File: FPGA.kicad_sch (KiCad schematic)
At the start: 14 parts, among them U3 XC7A100T-FTG256, U5 S25FL127S

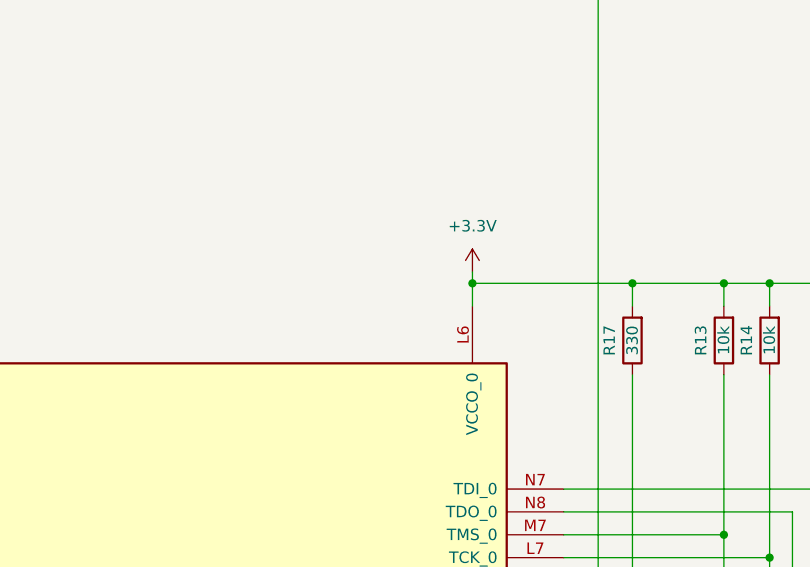
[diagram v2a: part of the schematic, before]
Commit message: Wired FPGA program to MCU
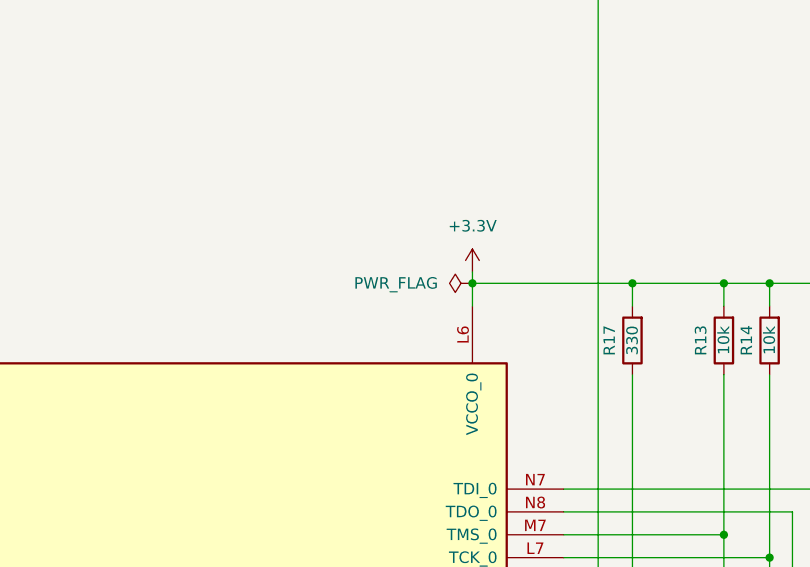
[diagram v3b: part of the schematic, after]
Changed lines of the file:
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@@
+    )
+  )
+  (symbol (lib_id "power:PWR_FLAG") (at 91.44 182.88 90) (unit 1)
+    (in_bom yes) (on_board yes) (dnp no) (fields_autoplaced)
+    (property "Reference" "#FLG04" (at 89.535 182.88 0)
+      (effects (font (size 1.27 1.27)) hide)
+    )
+    (property "Value" "PWR_FLAG" (at 87.63 182.88 90)
+      (effects (font (size 1.27 1.27)) (justify left))
+    )
+    (property "Footprint" "" (at 91.44 182.88 0)
+      (effects (font (size 1.27 1.27)) hide)
+    )
+    (property "Datasheet" "~" (at 91.44 182.88 0)
+      (effects (font (size 1.27 1.27)) hide)
+    )
+    (pin "1")
+    (instances
+      (project "GuitarZero"
+        (path "/fba50eda-8593-4456-af98-ff56fd418a76/7788bc9b-1e55-4835-b7d3-ea790efb8c61"
+          (reference "#FLG04") (unit 1)
+        )
+      )
     )
   )

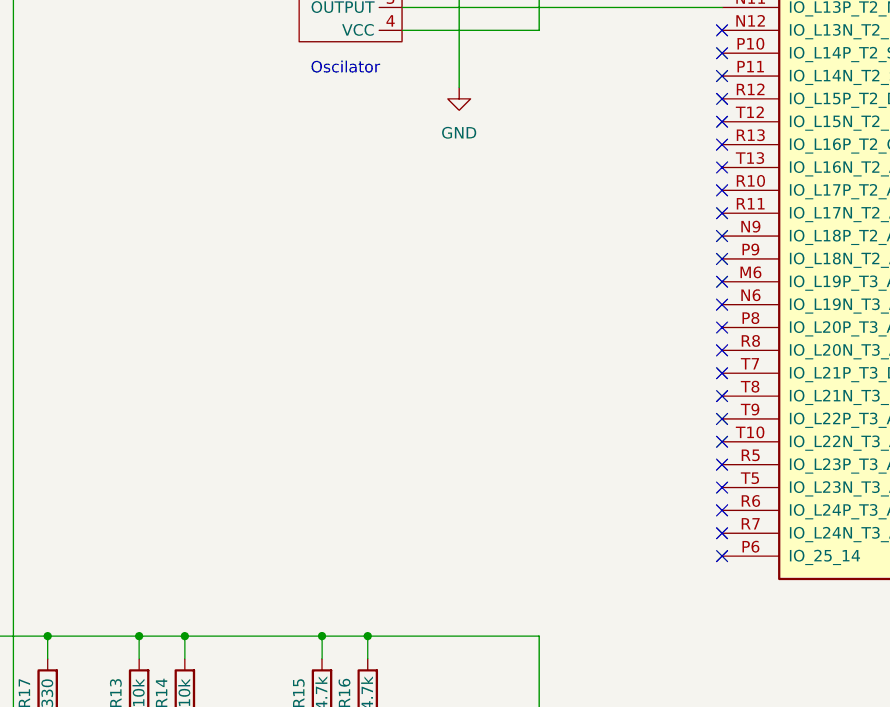
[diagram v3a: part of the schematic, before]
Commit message: Added 16 pins of GPIO backups to FPGA
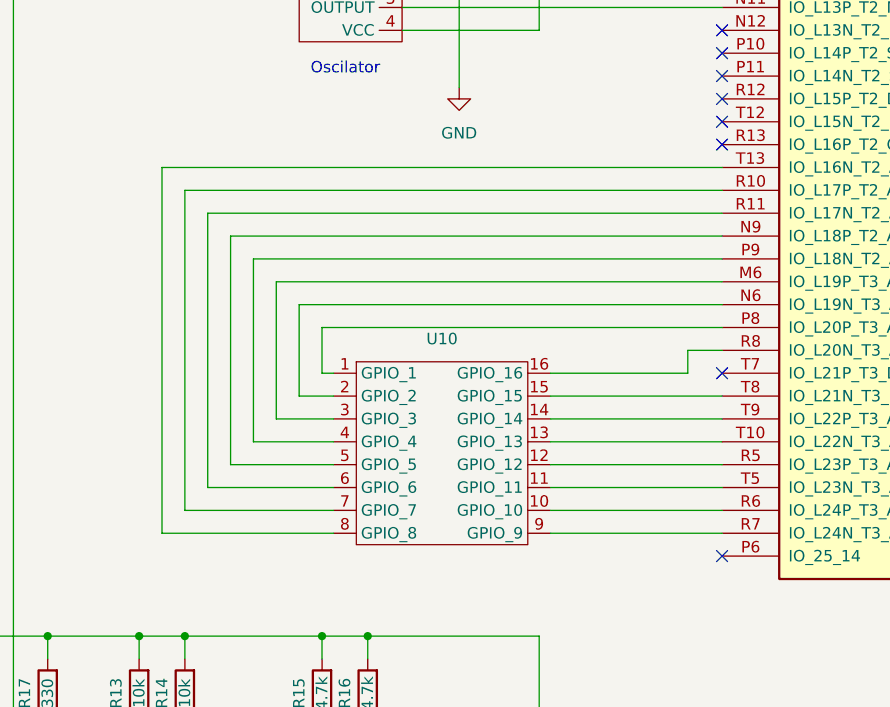
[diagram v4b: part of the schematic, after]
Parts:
- added U10: ~, symbol GuitarZero:GPIO_Pins
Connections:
- net at U3.M6 (IO_L19P_T3_A10_D26_14): now also U10.3 (GPIO_3)
- net at U3.N6 (IO_L19N_T3_A09_D25_VREF_14): now also U10.2 (GPIO_2)
- net at U3.N9 (IO_L18P_T2_A12_D28_14): now also U10.5 (GPIO_5)
- net at U3.P8 (IO_L20P_T3_A08_D24_14): now also U10.1 (GPIO_1)
- net at U3.P9 (IO_L18N_T2_A11_D27_14): now also U10.4 (GPIO_4)
- net at U3.R10 (IO_L17P_T2_A14_D30_14): now also U10.7 (GPIO_7)
- net at U3.R11 (IO_L17N_T2_A13_D29_14): now also U10.6 (GPIO_6)
- net at U3.R5 (IO_L23P_T3_A03_D19_14): now also U10.12 (GPIO_12)
- net at U3.R6 (IO_L24P_T3_A01_D17_14): now also U10.10 (GPIO_10)
- net at U3.R7 (IO_L24N_T3_A00_D16_14): now also U10.9 (GPIO_9)
- net at U3.R8 (IO_L20N_T3_A07_D23_14): now also U10.16 (GPIO_16)
- net at U3.T10 (IO_L22N_T3_A04_D20_14): now also U10.13 (GPIO_13)
- net at U3.T13 (IO_L16N_T2_A15_D31_14): now also U10.8 (GPIO_8)
- net at U3.T5 (IO_L23N_T3_A02_D18_14): now also U10.11 (GPIO_11)
- net at U3.T8 (IO_L21N_T3_DQS_A06_D22_14): now also U10.15 (GPIO_15)
- net at U3.T9 (IO_L22P_T3_A05_D21_14): now also U10.14 (GPIO_14)
- no-connect marks 159 -> 143

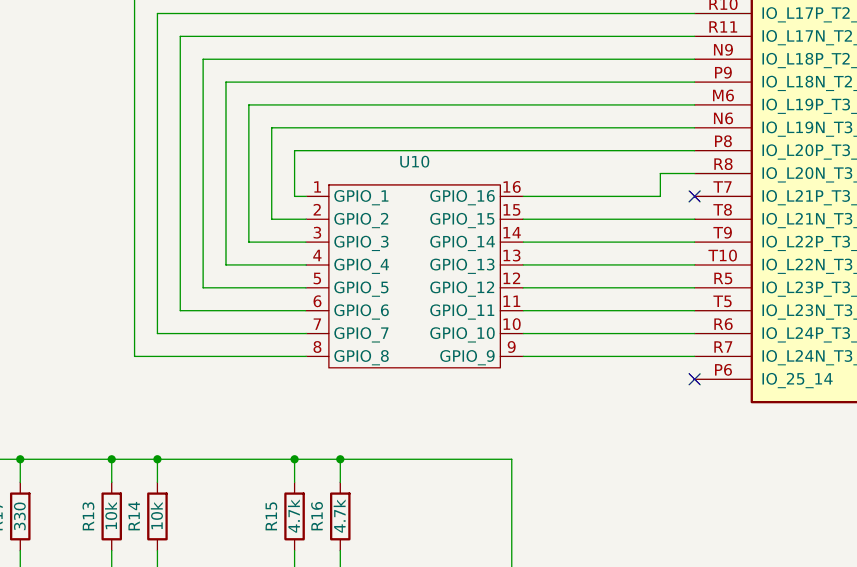
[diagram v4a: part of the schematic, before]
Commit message: Added final GPIO_pins
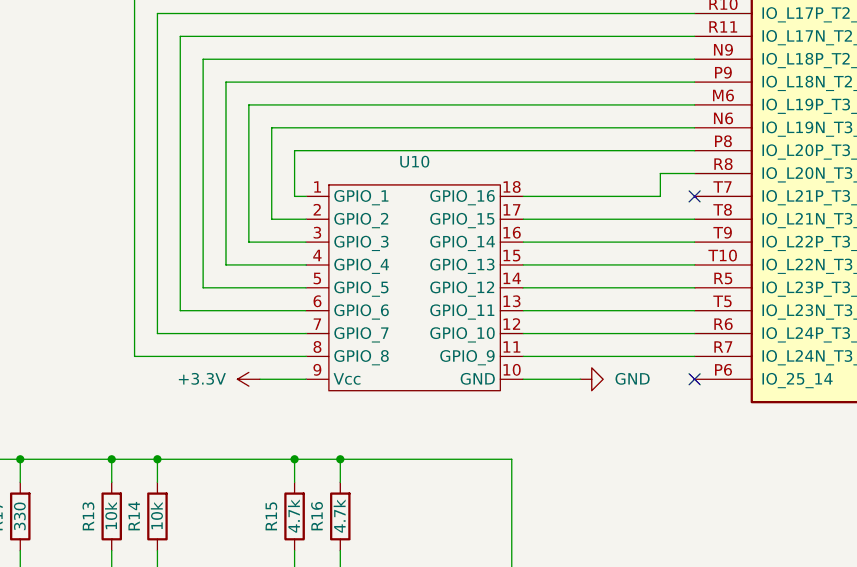
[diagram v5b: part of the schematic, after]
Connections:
- net +3.3V: now also U10.9 (Vcc)
- net GND: now also U10.10 (GND)
- net at U3.R6 (IO_L24P_T3_A01_D17_14): now also U10.12 (GPIO_10); no longer U10.10 (GPIO_10)
- net at U10.11 (GPIO_9): now also U3.R7 (IO_L24N_T3_A00_D16_14); no longer U3.T5 (IO_L23N_T3_A02_D18_14)
- net at U3.R5 (IO_L23P_T3_A03_D19_14): now also U10.14 (GPIO_12); no longer U10.12 (GPIO_12)
- net at U3.T10 (IO_L22N_T3_A04_D20_14): now also U10.15 (GPIO_13); no longer U10.13 (GPIO_13)
- net at U3.T9 (IO_L22P_T3_A05_D21_14): now also U10.16 (GPIO_14); no longer U10.14 (GPIO_14)
- net at U3.T8 (IO_L21N_T3_DQS_A06_D22_14): now also U10.17 (GPIO_15); no longer U10.15 (GPIO_15)
- net at U3.R8 (IO_L20N_T3_A07_D23_14): now also U10.18 (GPIO_16); no longer U10.16 (GPIO_16)
- new net: U10.13 (GPIO_11), U3.T5 (IO_L23N_T3_A02_D18_14)

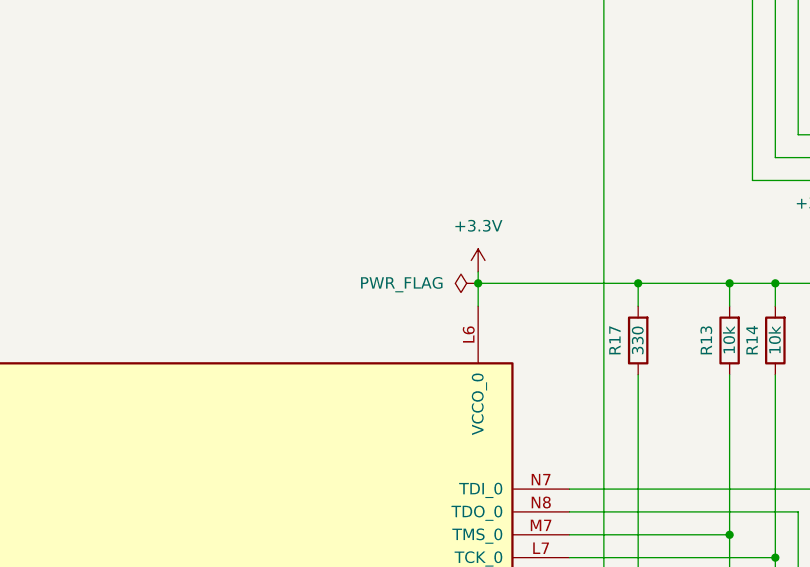
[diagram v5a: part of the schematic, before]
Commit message: Now follows with Electrical Rules
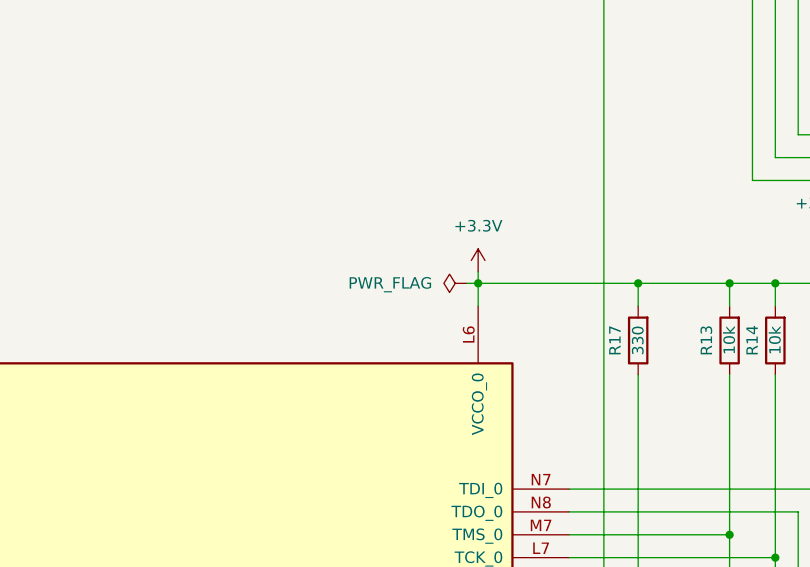
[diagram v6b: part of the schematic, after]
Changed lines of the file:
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@@
+    (stroke (width 0) (type default))
+  )
+  (wire (pts (xy 90.17 182.88) (xy 91.44 182.88))
     (stroke (width 0) (type default))
   )
@@
     )
   )
-  (symbol (lib_id "power:PWR_FLAG") (at 91.44 182.88 90) (unit 1)
+  (symbol (lib_id "power:PWR_FLAG") (at 90.17 182.88 90) (unit 1)
     (in_bom yes) (on_board yes) (dnp no) (fields_autoplaced)
-    (property "Reference" "#FLG04" (at 89.535 182.88 0)
-      (effects (font (size 1.27 1.27)) hide)
-    )
-    (property "Value" "PWR_FLAG" (at 87.63 182.88 90)
+    (property "Reference" "#FLG04" (at 88.265 182.88 0)
+      (effects (font (size 1.27 1.27)) hide)
+    )
+    (property "Value" "PWR_FLAG" (at 86.36 182.88 90)
       (effects (font (size 1.27 1.27)) (justify left))
     )
-    (property "Footprint" "" (at 91.44 182.88 0)
-      (effects (font (size 1.27 1.27)) hide)
-    )
-    (property "Datasheet" "~" (at 91.44 182.88 0)
-      (effects (font (size 1.27 1.27)) hide)
-    )
+    (property "Footprint" "" (at 90.17 182.88 0)
+      (effects (font (size 1.27 1.27)) hide)
+    )
+    (property "Datasheet" "~" (at 90.17 182.88 0)
+      (effects (font (size 1.27 1.27)) hide)
+    )
